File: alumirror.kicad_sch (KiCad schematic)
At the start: 35 parts, among them J1 USB_C_Receptacle_USB2.0_16P_2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, J2 USB_C_Receptacle_USB2.0_16P_2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, J3 USB_C_Receptacle_USB2.0_16P_2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, J4 USB_C_Receptacle_USB2.0_16P_2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, SW1 BOOT, U1 CH552T, U2 CH552T, U3 USBLC6-2P6, U4 USBLC6-2P6, U5 USBLC6-2P6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

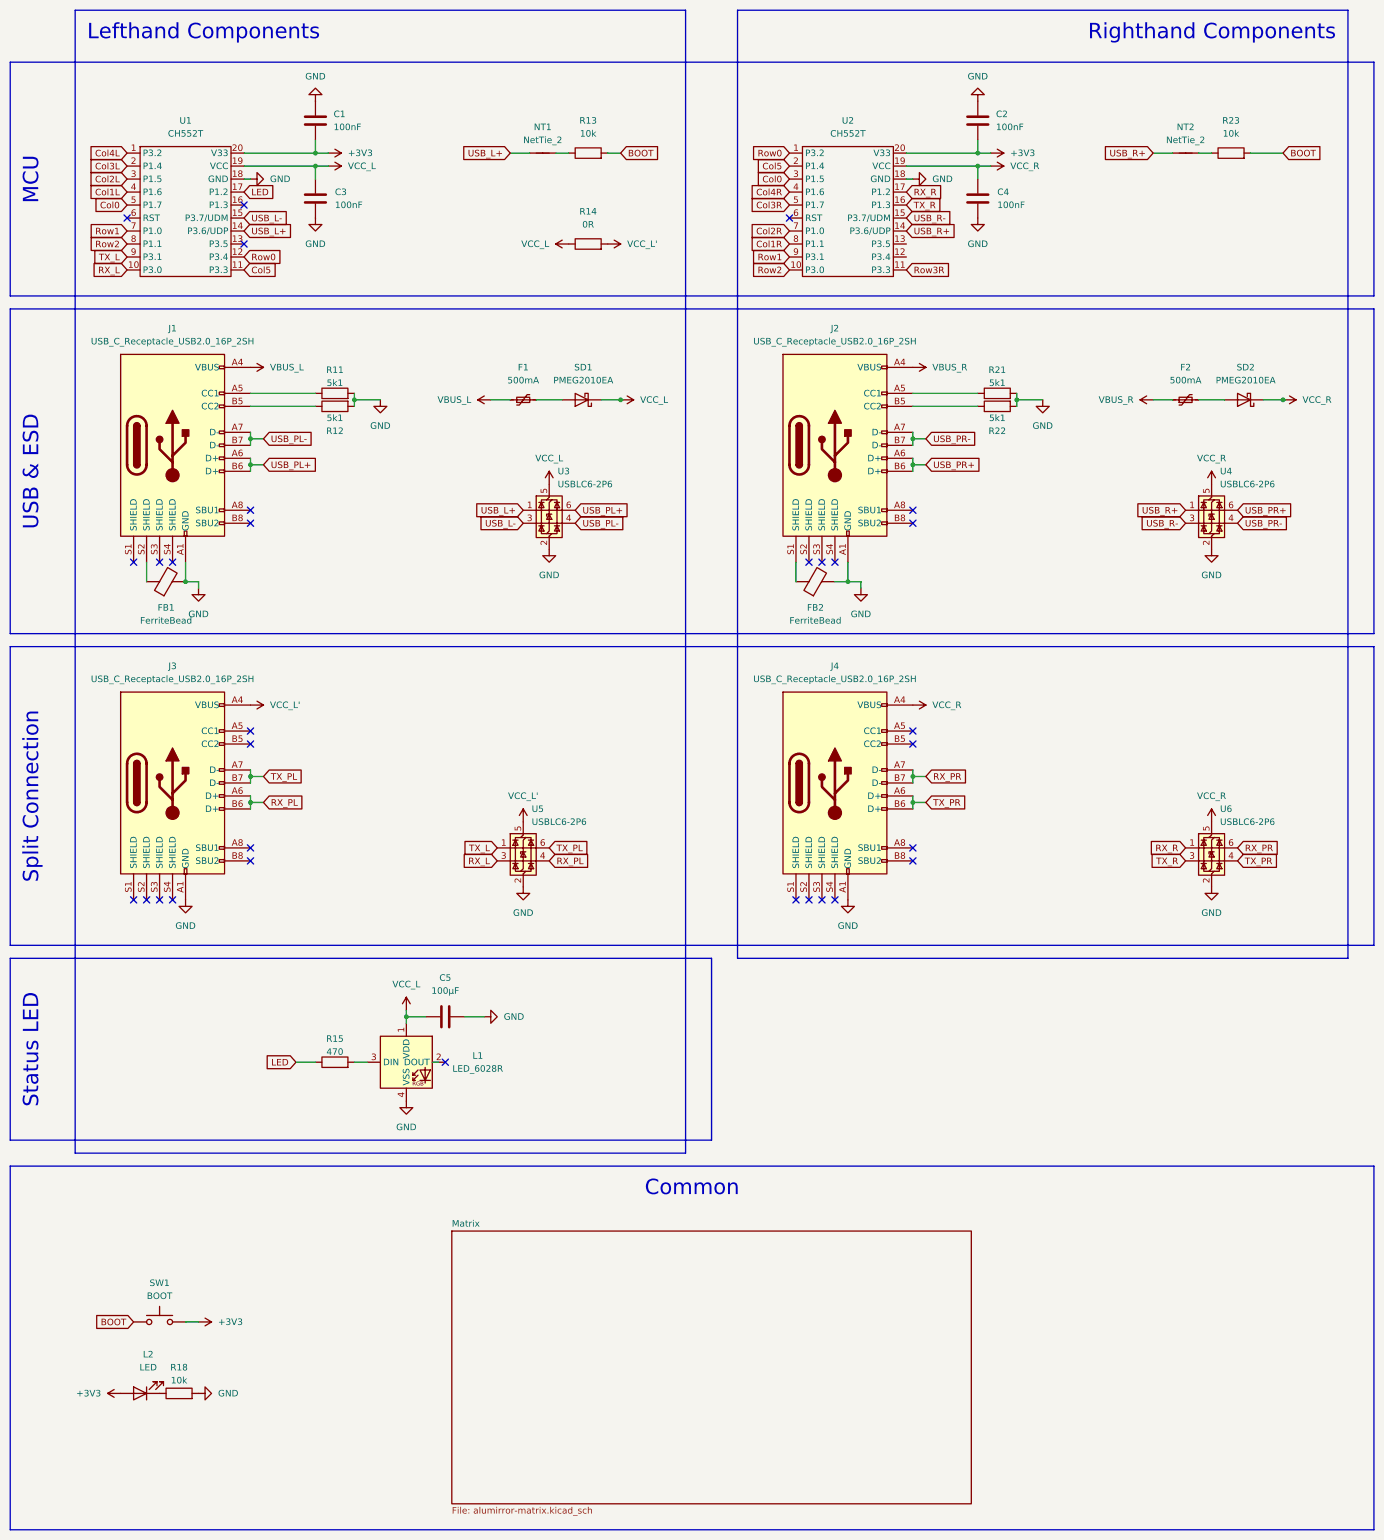
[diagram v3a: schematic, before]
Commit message: Refine middle layer 3D print cutouts
Also renumber diodes — D0# are now DO# and SD1 and SD2 are and D2
Add diode (D3) on VCC line to RGB LED (this drops VCC to ~4V, which is still within spec., but now closer to the 3.3V control signal as DIN should be VCC±0.5V).
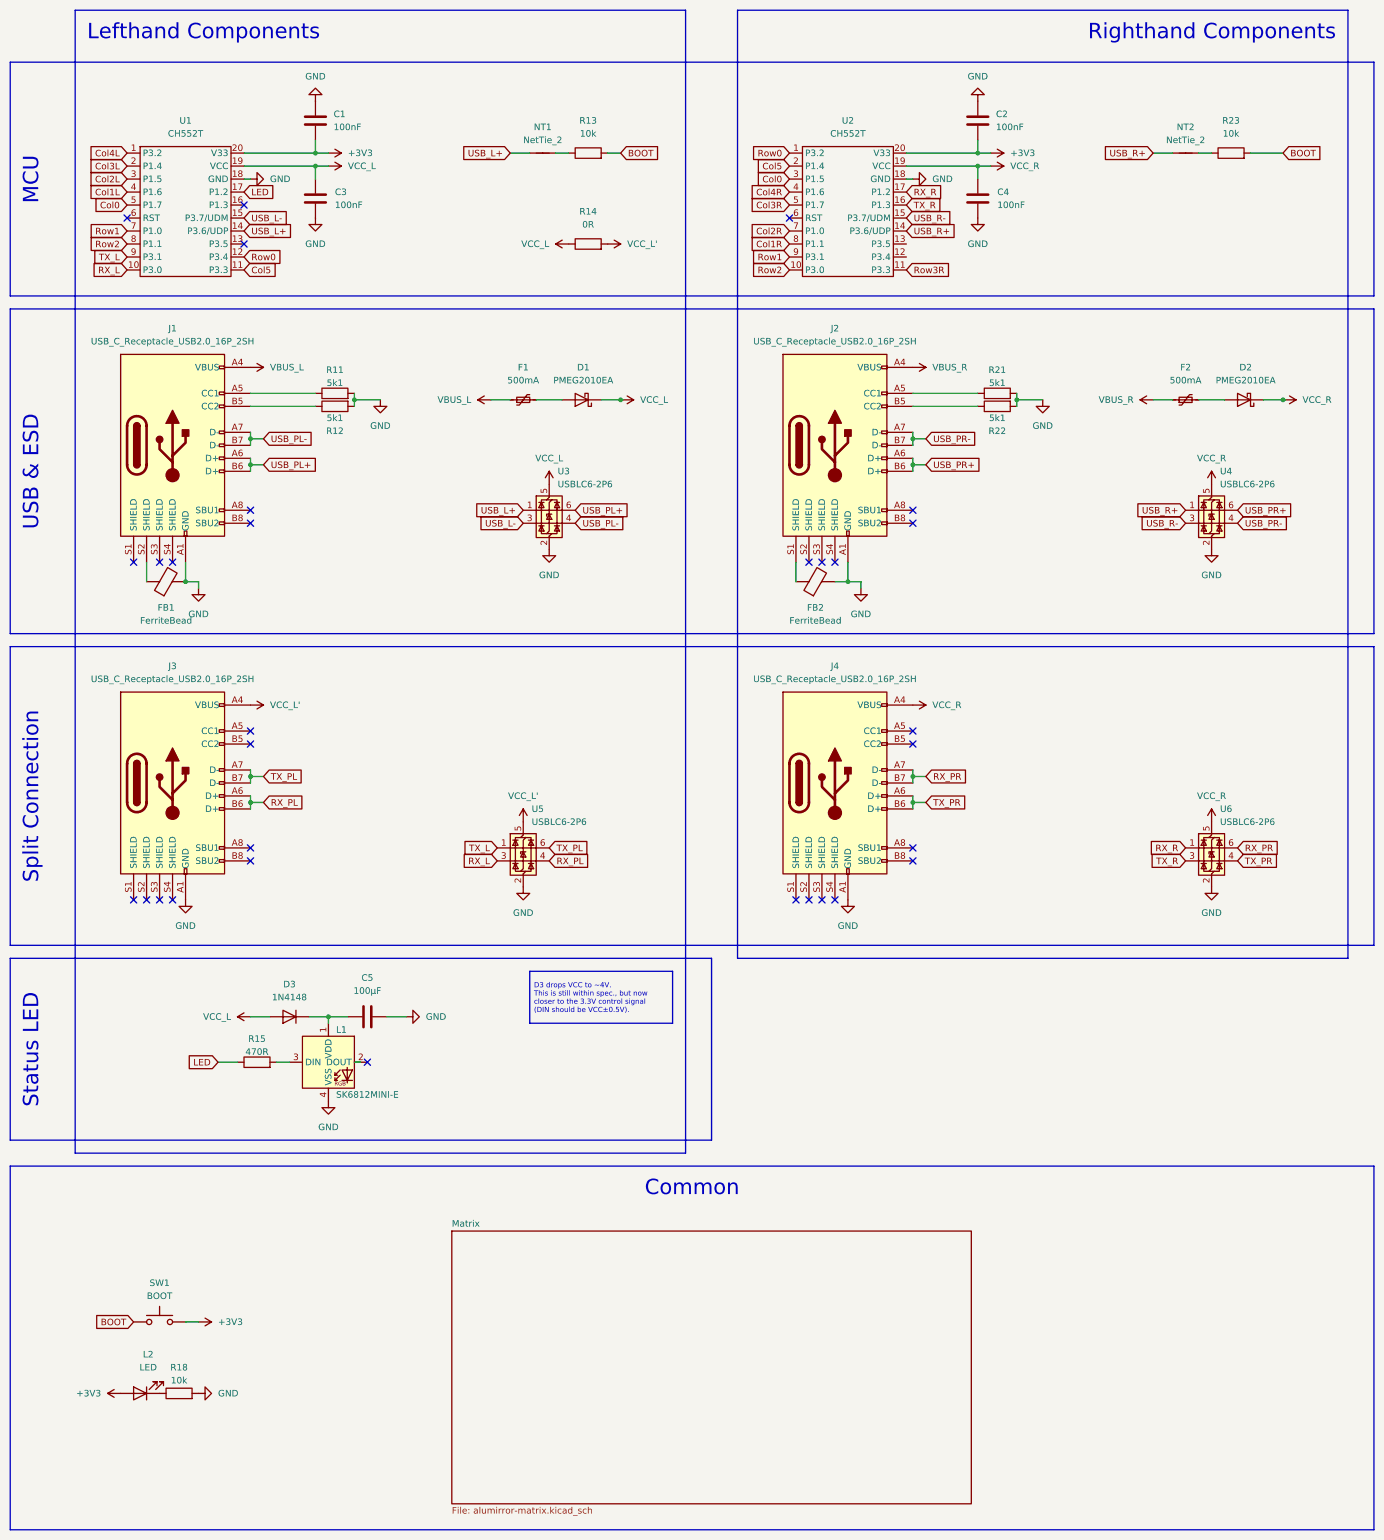
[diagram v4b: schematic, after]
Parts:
- added D3: 1N4148, Project Library:D_SOD-123_Mod, symbol Device:D
- L1: value LED_6028R -> SK6812MINI-E
- R11, R12, R13, R18, R21, R22, R23: footprint Project Library:R_0603_1608Metric_Mod -> Resistor_SMD:R_0603_1608Metric
- R14: footprint Project Library:R_2010_5025Metric_Mod -> Resistor_SMD:R_2010_5025Metric
- R15: value 470 -> 470R; footprint Project Library:R_0603_1608Metric_Mod -> Resistor_SMD:R_0603_1608Metric
- renumbered SD1 to D1, SD2 to D2
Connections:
- net VCC_L: now also D3.2 (A); no longer C5.1, L1.1 (VDD)
- new net: C5.1, D3.1 (K), L1.1 (VDD)
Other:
- moved on the sheet: C5, L1, R15

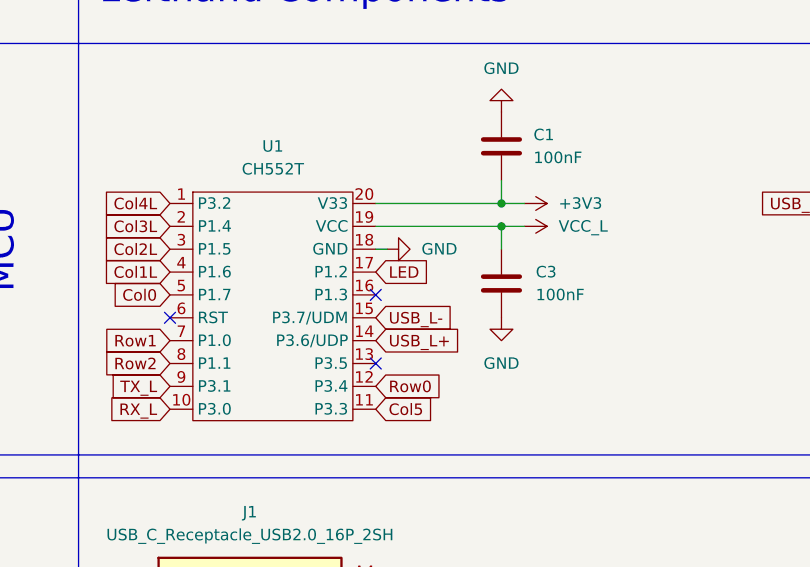
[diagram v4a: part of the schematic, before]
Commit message: Switch RGB LED capacitor (C5) and resistor (R15) to 0805 size
Found some 0805 470Ω resistors in the parts bin, and this size is a bit less ridiculously small than 0603.
Also, switched LED pin to P1.3 for better spacing and fixed (now) unnecessary misalignment of R13.
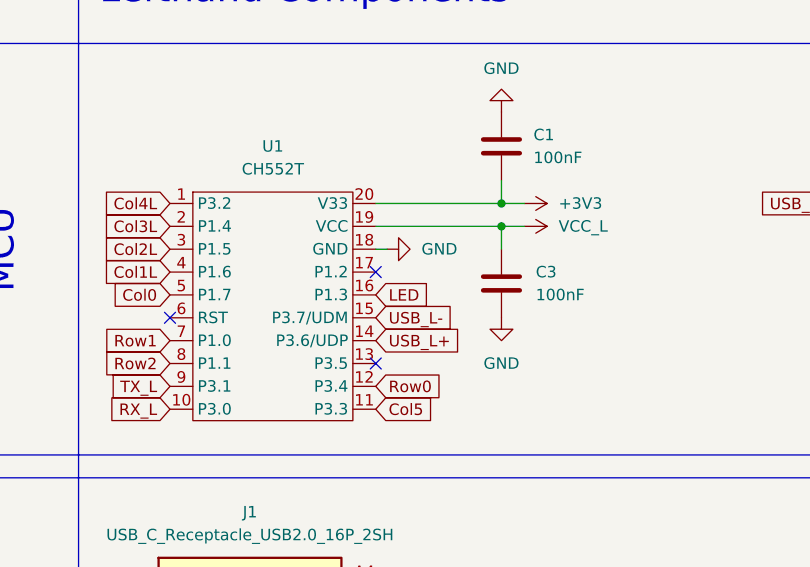
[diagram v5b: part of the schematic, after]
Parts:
- C5: footprint Capacitor_SMD:C_0603_1608Metric -> Capacitor_SMD:C_0805_2012Metric
- R15: footprint Resistor_SMD:R_0603_1608Metric -> Resistor_SMD:R_0805_2012Metric
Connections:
- net LED: now also U1.16 (P1.3); no longer U1.17 (P1.2)
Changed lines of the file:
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@@
 	)
 	(no_connect
-		(at 60.96 53.34)
+		(at 60.96 50.8)
 	)
 	(no_connect
@@
 	(global_label "LED"
 		(shape input)
-		(at 60.96 50.8 0)
+		(at 60.96 53.34 0)
 		(fields_autoplaced yes)
 		(effects
@@
 		)
 		(property "Intersheetrefs" "${INTERSHEET_REFS}"
-			(at 67.3923 50.8 0)
+			(at 67.3923 53.34 0)
 			(effects
 				(font
@@
 			)
 		)
-		(property "Footprint" "Capacitor_SMD:C_0603_1608Metric"
+		(property "Footprint" "Capacitor_SMD:C_0805_2012Metric"
 			(at 88.9 211.1248 0)
 			(effects
@@
 			)
 		)
-		(property "Footprint" "Resistor_SMD:R_0603_1608Metric"
+		(property "Footprint" "Resistor_SMD:R_0805_2012Metric"
 			(at 63.5 222.758 90)
 			(effects

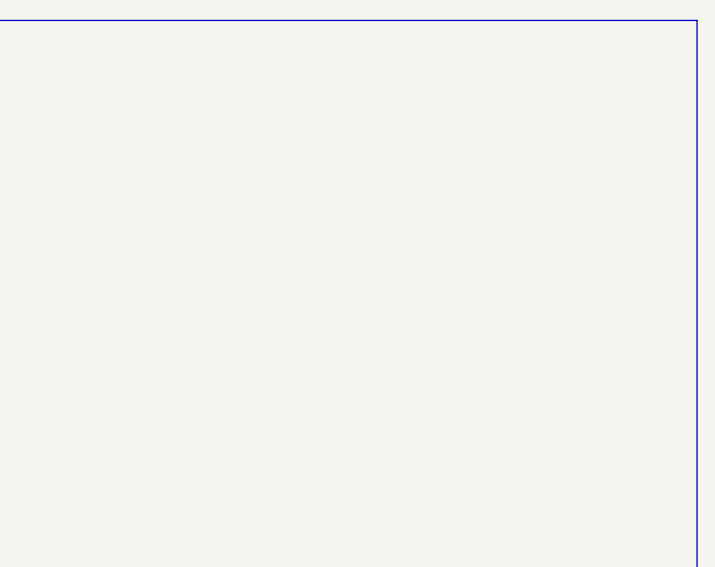
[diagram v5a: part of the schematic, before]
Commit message: Add mounting holes and re-route tracks around them
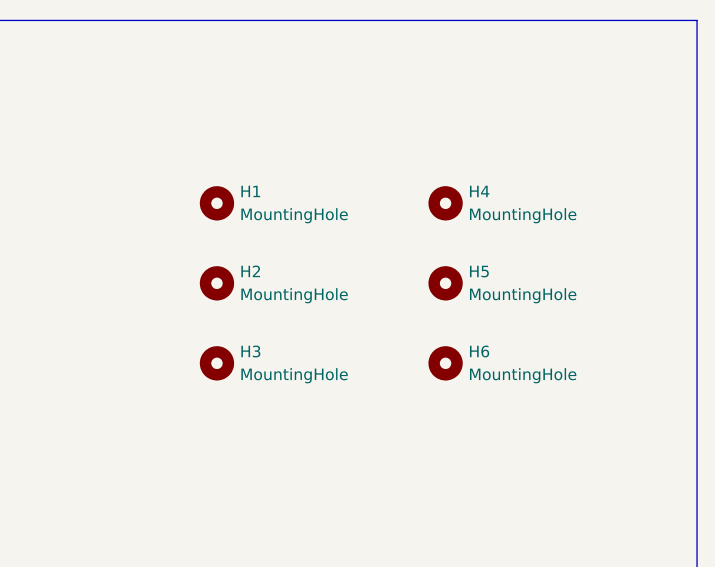
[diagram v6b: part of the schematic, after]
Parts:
- added H1, H2, H3, H4, H5, H6: MountingHole, Project Library:MountingHole_2.2mm_M2_SMD_Solder_Nut, symbol Mechanical:MountingHole

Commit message: Create another custom SOD-123 footprint
This one has the thicker polarity line of the existing modification, but without the 3D layer cutout.
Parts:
- D3: footprint Project Library:D_SOD-123_Mod -> Project Library:D_SOD-123
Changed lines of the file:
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@@
 			)
 		)
-		(property "Footprint" "Project Library:D_SOD-123_Mod"
+		(property "Footprint" "Project Library:D_SOD-123"
 			(at 69.85 212.09 0)
 			(effects

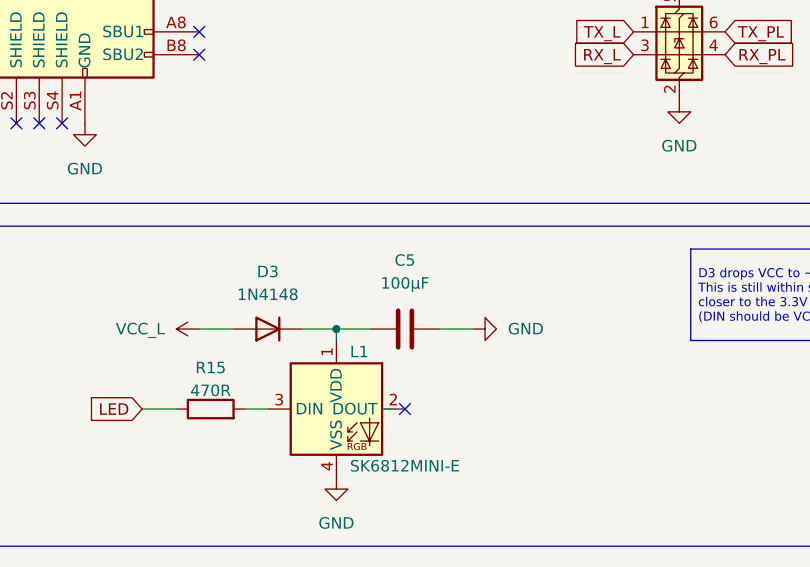
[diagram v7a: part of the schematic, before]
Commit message: Change RGB LED decoupling capacitor (C5)
Use 100nF — there seems to be some contradictory information on this, but this seems to be the consensus.
Use 0603 size since the capacitance now matches C1–4, which are this size.
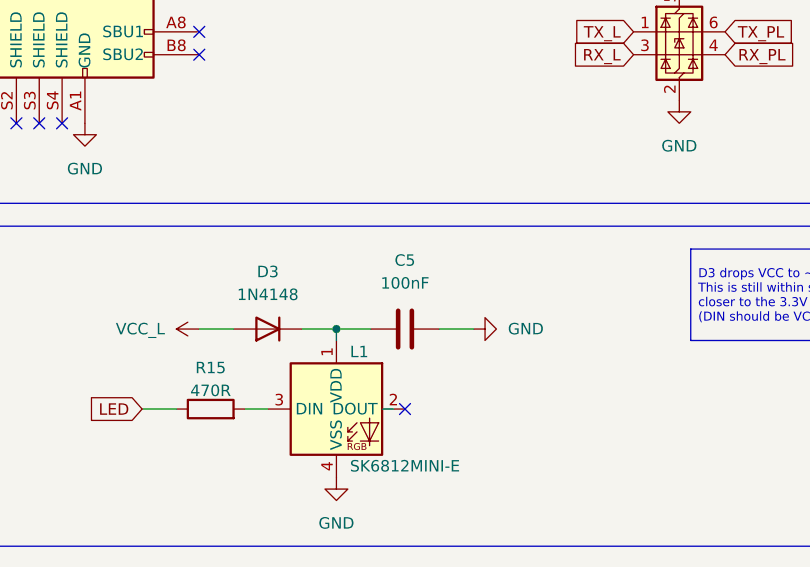
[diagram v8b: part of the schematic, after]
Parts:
- C5: value 100µF -> 100nF; footprint Capacitor_SMD:C_0805_2012Metric -> Capacitor_SMD:C_0603_1608Metric
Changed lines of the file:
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@@
+	)
+	(symbol
+		(lib_id "Device:C")
+		(at 85.09 212.09 90)
+		(unit 1)
+		(exclude_from_sim no)
+		(in_bom yes)
+		(on_board yes)
+		(dnp no)
+		(fields_autoplaced yes)
+		(property "Reference" "C5"
+			(at 85.09 204.47 90)
+			(effects
+				(font
+					(size 1.27 1.27)
+				)
+			)
+		)
+		(property "Value" "100nF"
+			(at 85.09 207.01 90)
+			(effects
+				(font
+					(size 1.27 1.27)
+				)
+			)
+		)
+		(property "Footprint" "Capacitor_SMD:C_0603_1608Metric"
+			(at 88.9 211.1248 0)
+			(effects
+				(font
+					(size 1.27 1.27)
+				)
+				(hide yes)
+			)
+		)
+		(property "Datasheet" "~"
+			(at 85.09 212.09 0)
+			(effects
+				(font
+					(size 1.27 1.27)
+				)
+				(hide yes)
+			)
+		)
+		(property "Description" ""
+			(at 85.09 212.09 0)
+			(effects
+				(font
+					(size 1.27 1.27)
+				)
+				(hide yes)
+			)
+		)
+		(property "LCSC" "C66501"
+			(at 85.09 212.09 0)
+			(effects
+				(font
+					(size 1.27 1.27)
+				)
+				(hide yes)
+			)
+		)
+		(property "DigiKey" "1276-1005"
+			(at 85.09 212.09 0)
+			(effects
+				(font
+					(size 1.27 1.27)
+				)
+				(hide yes)
+			)
+		)
+		(pin "1"
+		)
+		(pin "2"
+		)
+		(instances
+			(project "alumirror"
+				(path "/52f043ac-ccff-4c85-bc10-2db9d3c9e3f3"
+					(reference "C5")
+					(unit 1)
+				)
+			)
+		)
 	)
 	(symbol
@@
 					(unit 1)
 				)
-			)
-		)
-	)
-	(symbol
-		(lib_id "Device:C")
-		(at 85.09 212.09 90)
-		(unit 1)
-		(exclude_from_sim no)
-		(in_bom yes)
-		(on_board yes)
-		(dnp no)
-		(fields_autoplaced yes)
-		(property "Reference" "C5"
-			(at 85.09 204.47 90)
-			(effects
-				(font
-					(size 1.27 1.27)
-				)
-			)
-		)
-		(property "Value" "100µF"
-			(at 85.09 207.01 90)
-			(effects
-				(font
-					(size 1.27 1.27)
-				)
-			)
-		)
-		(property "Footprint" "Capacitor_SMD:C_0805_2012Metric"
-			(at 88.9 211.1248 0)
-			(effects
-				(font
-					(size 1.27 1.27)
-				)
-				(hide yes)
-			)
-		)
-		(property "Datasheet" "~"
-			(at 85.09 212.09 0)
-			(effects
-				(font
-					(size 1.27 1.27)
-				)
-				(hide yes)
-			)
-		)
-		(property "Description" ""
-			(at 85.09 212.09 0)
-			(effects
-				(font
-					(size 1.27 1.27)
-				)
-				(hide yes)
-			)
-		)
-		(property "LCSC" "C66501"
-			(at 85.09 212.09 0)
-			(effects
-				(font
-					(size 1.27 1.27)
-				)
-				(hide yes)
-			)
-		)
-		(property "DigiKey" "1276-1005"
-			(at 85.09 212.09 0)
-			(effects
-				(font
-					(size 1.27 1.27)
-				)
-				(hide yes)
-			)
-		)
-		(pin "1"
-		)
-		(pin "2"
-		)
-		(instances
-			(project "alumirror"
-				(path "/52f043ac-ccff-4c85-bc10-2db9d3c9e3f3"
-					(reference "C5")
-					(unit 1)
-				)
